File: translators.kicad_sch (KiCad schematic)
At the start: 56 parts, among them Q5 DMG1012T-7, U12 SN74AXC8T245RJWR, U2 SN74AXC8T245RJWR, U3 SN74AXC8T245RJWR, U4 SN74AXC8T245RJWR, U5 SN74AXC8T245RJWR, U6 SN74AXC8T245RJWR

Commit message: [#52835] schematics: update LPDDR5 connections, finish translators subsheet
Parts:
- removed C23, C24, C25, C27, C28, C29: C_1u_0402, antmicro-footprints:C_0402_1005Metric, symbol antmicroCapacitors0402:C_1u_0402
- removed Q5: DMG1012T-7, antmicro-footprints:SOT-523, symbol antmicroTransistorsFETsMOSFETsSingle:DMG1012T-7
- removed R1, R10, R2, R3, R4, R5, R50, R51, R52, R53, R54, R55, R6, R9: 4x0R_0402_array, antmicro-footprints:4x0R_0402_array_EXB28V, symbol antmicroResistorNetworksArrays:4x0R_0402_array
- removed R20, R59, R62, R67: R_0R_0402, antmicro-footprints:R_0402_1005Metric, symbol antmicroResistors0402:R_0R_0402
- removed R70, R71: R_1k_0402, antmicro-footprints:R_0402_1005Metric, symbol antmicroResistors0402:R_1k_0402
- removed U2, U4, U5: SN74AXC8T245RJWR, antmicro-footprints:UQFN-28-2x4mm_P0.4mm_Texas_RJW0024A, symbol antmicroLogicTranslatorsLevelShifters:SN74AXC8T245RJWR
- added C? (x6): C_1u_0402, antmicro-footprints:C_0402_1005Metric, symbol antmicroCapacitors0402:C_1u_0402
- added R? (x14): 4x0R_0402_array, antmicro-footprints:4x0R_0402_array_EXB28V, symbol antmicroResistorNetworksArrays:4x0R_0402_array
- added R? (x4): R_0R_0402, antmicro-footprints:R_0402_1005Metric, symbol antmicroResistors0402:R_0R_0402
- added U? (x3): SN74AXC8T245RJWR, antmicro-footprints:UQFN-28-2x4mm_P0.4mm_Texas_RJW0024A, symbol antmicroLogicTranslatorsLevelShifters:SN74AXC8T245RJWR
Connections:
- net DQA_{VTI}0: now also R?.5 (R4.2), U?.9 (A8)
- net DQA_{VTI}1: now also R?.6 (R3.2), U?.8 (A7)
- net DQA_{VTI}10: now also R?.6 (R3.2), U?.4 (A3)
- net DQA_{VTI}11: now also R?.5 (R4.2), U?.5 (A4)
- net DQA_{VTI}12: now also R?.8 (R1.2), U?.6 (A5)
- net DQA_{VTI}13: now also R?.7 (R2.2), U?.7 (A6)
- net DQA_{VTI}14: now also R?.6 (R3.2), U?.8 (A7)
- net DQA_{VTI}15: now also R?.5 (R4.2), U?.9 (A8)
- net DQA_{VTI}2: now also R?.7 (R2.2), U?.7 (A6)
- net DQA_{VTI}3: now also R?.8 (R1.2), U?.6 (A5)
- net DQA_{VTI}4: now also R?.5 (R4.2), U?.5 (A4)
- net DQA_{VTI}5: now also R?.6 (R3.2), U?.4 (A3)
- net DQA_{VTI}6: now also R?.7 (R2.2), U?.3 (A2)
- net DQA_{VTI}7: now also R?.8 (R1.2), U?.2 (A1)
- net DQA_{VTI}8: now also R?.8 (R1.2), U?.2 (A1)
- net DQA_{VTI}9: now also R?.7 (R2.2), U?.3 (A2)
- net DQA_{VT}0: now also R?.4 (R4.1), U?.13 (B8)
- net DQA_{VT}1: now also R?.3 (R3.1), U?.14 (B7)
- net DQA_{VT}10: now also R?.3 (R3.1), U?.18 (B3)
- net DQA_{VT}11: now also R?.4 (R4.1), U?.17 (B4)
- net DQA_{VT}12: now also R?.1 (R1.1), U?.16 (B5)
- net DQA_{VT}13: now also R?.2 (R2.1), U?.15 (B6)
- net DQA_{VT}14: now also R?.3 (R3.1), U?.14 (B7)
- net DQA_{VT}15: now also R?.4 (R4.1), U?.13 (B8)
- net DQA_{VT}2: now also R?.2 (R2.1), U?.15 (B6)
- net DQA_{VT}3: now also R?.1 (R1.1), U?.16 (B5)
- net DQA_{VT}4: now also R?.4 (R4.1), U?.17 (B4)
- net DQA_{VT}5: now also R?.3 (R3.1), U?.18 (B3)
- net DQA_{VT}6: now also R?.2 (R2.1), U?.19 (B2)
- net DQA_{VT}7: now also R?.1 (R1.1), U?.20 (B1)
- net DQA_{VT}8: now also R?.1 (R1.1), U?.20 (B1)
- net DQA_{VT}9: now also R?.2 (R2.1), U?.19 (B2)
- net DQH_DIR: now also U?.1 (DIR1)
- net DQL_DIR: now also U?.1 (DIR1)
- net FPGA_VDDQ: now also C?.2, C?.2, C?.2, R?.2, U?.24 (VCCA), U?.24 (VCCA), U?.24 (VCCA)
- net GND: now also R61.2, C?.1, C?.1, C?.1, C?.1, C?.1, C?.1, R?.1 (R1.1), R?.2, R?.6 (R3.2), R?.7 (R2.2), R?.7 (R2.2), R?.8 (R1.2), R?.8 (R1.2), R?.8 (R1.2), U?.11 (GND), U?.11 (GND), U?.11 (GND), U?.12 (GND), U?.12 (GND), U?.12 (GND); no longer R61.1
- net VDD_TL: now also C?.2, C?.2, C?.2, U?.22 (VCCB), U?.22 (VCCB), U?.22 (VCCB), U?.23 (VCCB), U?.23 (VCCB), U?.23 (VCCB)
- net ~{TRANS_OE_2}: now also R?.2, U?.21 (OE_N), U?.21 (OE_N), U?.21 (OE_N)
- net ~{TRANS_OE}: now also R?.1
- net at R23.2: now also U?.10 (DIR2)
- net at U12.1 (DIR1): now also R?.1
- net at U12.10 (DIR2): now also R?.1
- net at U6.1 (DIR1): now also R61.1; no longer R61.2
- net at U6.14 (B7): now also R?.3 (R3.1)
- net at U6.15 (B6): now also R?.2 (R2.1)
- net at U6.16 (B5): now also R?.1 (R1.1)
- net at U6.19 (B2): now also R?.2 (R2.1)
- net at U6.20 (B1): now also R?.1 (R1.1)
- net at R22.2: now also U?.10 (DIR2)
- net at R21.2: now also U?.10 (DIR2)
- net CK_A_{VTI}_N renamed CK_{VTI}_N
- net CK_A_{VTI}_P renamed CK_{VTI}_P
- net CK_A_{VT}_N renamed CK_{VT}_N
- net CK_A_{VT}_P renamed CK_{VT}_P
- net CS_{VTI}_A0 renamed CS_{VTI}0
- net CS_{VTI}_A1 renamed CS_{VTI}1
- net CS_{VT}_A0 renamed CS_{VT}0
- net CS_{VT}_A1 renamed CS_{VT}1
- net DMI_A1_DIR renamed DMI1_DIR
- net DMI_{VTI}_A0 renamed DMI_{VTI}0
- net DMI_{VTI}_A1 renamed DMI_{VTI}1
- net DMI_{VT}_A0 renamed DMI_{VT}0
- net DMI_{VT}_A1 renamed DMI_{VT}1
- net DMI_{VT}1: now also R?.4 (R4.1)
- net LPDDR5.CK_A_N renamed LPDDR5.CK_N
- net LPDDR5.CK_A_P renamed LPDDR5.CK_P
- net LPDDR5.CS_A0 renamed LPDDR5.CS0
- net LPDDR5.CS_A1 renamed LPDDR5.CS1
- net LPDDR5.DMI_A0 renamed LPDDR5.DMI0
- net LPDDR5.RDQS_A_0_N renamed LPDDR5.RDQS0_N
- net LPDDR5.RDQS_A_0_P renamed LPDDR5.RDQS0_P
- net LPDDR5.WCK_A_0_N renamed LPDDR5.WCK0_N
- net LPDDR5.WCK_A_0_P renamed LPDDR5.WCK0_P
- net LPDDR5.WCK_A_1_N renamed LPDDR5.WCK1_N
- net LPDDR5.WCK_A_1_P renamed LPDDR5.WCK1_P
- net LPDDR5_HV.CK_A_N renamed LPDDR5_HV.CK_N
- net LPDDR5_HV.CK_A_P renamed LPDDR5_HV.CK_P
- net LPDDR5_HV.CS_A0 renamed LPDDR5_HV.CS0
- net LPDDR5_HV.CS_A1 renamed LPDDR5_HV.CS1
- net LPDDR5_HV.DMI_A0 renamed LPDDR5_HV.DMI0
- net LPDDR5_HV.DMI_A1 renamed LPDDR5_HV.DMI1
- net LPDDR5_HV.RDQS_A_0_N renamed LPDDR5_HV.RDQS0_N
- net LPDDR5_HV.RDQS_A_0_P renamed LPDDR5_HV.RDQS0_P
- net LPDDR5_HV.RDQS_A_1_N renamed LPDDR5_HV.RDQS1_N
- net LPDDR5_HV.RDQS_A_1_P renamed LPDDR5_HV.RDQS1_P
- net LPDDR5_HV.WCK_A_0_N renamed LPDDR5_HV.WCK0_N
- net LPDDR5_HV.WCK_A_0_P renamed LPDDR5_HV.WCK0_P
- net LPDDR5_HV.WCK_A_1_N renamed LPDDR5_HV.WCK1_N
- net LPDDR5_HV.WCK_A_1_P renamed LPDDR5_HV.WCK1_P
- net RDQS_{VTI}_A0_N renamed RDQS_{VTI}0_N
- net RDQS_{VTI}_A0_P renamed RDQS_{VTI}0_P
- net RDQS_{VTI}_A1_N renamed RDQS_{VTI}1_N
- net RDQS_{VTI}_A1_P renamed RDQS_{VTI}1_P
- net RDQS_{VT}_A0_N renamed RDQS_{VT}0_N
- net RDQS_{VT}_A0_P renamed RDQS_{VT}0_P
- net RDQS_{VT}_A1_N renamed RDQS_{VT}1_N
- net RDQS_{VT}1_N: now also R?.4 (R4.1)
- net RDQS_{VT}_A1_P renamed RDQS_{VT}1_P
- net RDQS_{VT}1_P: now also R?.3 (R3.1)
- net WCK_A0_{VTI}_N renamed WCK0_{VTI}_N
- net WCK_A0_{VTI}_P renamed WCK0_{VTI}_P
- net WCK_A0_{VT}_N renamed WCK0_{VT}_N
- net WCK_A0_{VT}_P renamed WCK0_{VT}_P
- net WCK_A1_{VTI}_N renamed WCK1_{VTI}_N
- net WCK_A1_{VTI}_P renamed WCK1_{VTI}_P
- net WCK_A1_{VT}_N renamed WCK1_{VT}_N
- net WCK_A1_{VT}_P renamed WCK1_{VT}_P
- new net: R?.1 (R1.1), U?.20 (B1)
- new net: R?.1, U?.1 (DIR1)
- new net: R?.8 (R1.2), U?.2 (A1)
- new net CA_{VTI}0: R?.5 (R4.2), U?.9 (A8)
- new net CA_{VTI}1: R?.6 (R3.2), U?.8 (A7)
- new net CA_{VTI}2: R?.7 (R2.2), U?.7 (A6)
- new net CA_{VTI}3: R?.5 (R4.2), U?.5 (A4)
- new net CA_{VTI}4: R?.8 (R1.2), U?.6 (A5)
- new net CA_{VTI}5: R?.7 (R2.2), U?.3 (A2)
- new net CA_{VTI}6: R?.6 (R3.2), U?.4 (A3)
- new net CA_{VT}0: R?.4 (R4.1), U?.13 (B8)
- new net CA_{VT}1: R?.3 (R3.1), U?.14 (B7)
- new net CA_{VT}2: R?.2 (R2.1), U?.15 (B6)
- new net CA_{VT}3: R?.4 (R4.1), U?.17 (B4)
- new net CA_{VT}4: R?.1 (R1.1), U?.16 (B5)
- new net CA_{VT}5: R?.2 (R2.1), U?.19 (B2)
- new net CA_{VT}6: R?.3 (R3.1), U?.18 (B3)
- new net DMI0_DIR: R?.2
- new net LPDDR5.CA0: R?.5 (R4.2)
- new net LPDDR5.CA1: R?.6 (R3.2)
- new net LPDDR5.CA2: R?.7 (R2.2)
- new net LPDDR5.CA3: R?.5 (R4.2)
- new net LPDDR5.CA4: R?.8 (R1.2)
- new net LPDDR5.CA5: R?.7 (R2.2)
- new net LPDDR5.CA6: R?.6 (R3.2)
- new net LPDDR5.DMI1: R?.5 (R4.2)
- new net LPDDR5.DQ0: R?.5 (R4.2)
- new net LPDDR5.DQ1: R?.6 (R3.2)
- new net LPDDR5.DQ10: R?.6 (R3.2)
- new net LPDDR5.DQ11: R?.5 (R4.2)
- new net LPDDR5.DQ12: R?.8 (R1.2)
- new net LPDDR5.DQ13: R?.7 (R2.2)
- new net LPDDR5.DQ14: R?.6 (R3.2)
- new net LPDDR5.DQ15: R?.5 (R4.2)
- new net LPDDR5.DQ2: R?.7 (R2.2)
- new net LPDDR5.DQ3: R?.8 (R1.2)
- new net LPDDR5.DQ4: R?.5 (R4.2)
- new net LPDDR5.DQ5: R?.6 (R3.2)
- new net LPDDR5.DQ6: R?.7 (R2.2)
- new net LPDDR5.DQ7: R?.8 (R1.2)
- new net LPDDR5.DQ8: R?.8 (R1.2)
- new net LPDDR5.DQ9: R?.7 (R2.2)
- new net LPDDR5.RDQS1_N: R?.5 (R4.2)
- new net LPDDR5.RDQS1_P: R?.6 (R3.2)
- new net LPDDR5_HV.CA0: R?.4 (R4.1)
- new net LPDDR5_HV.CA1: R?.3 (R3.1)
- new net LPDDR5_HV.CA2: R?.2 (R2.1)
- new net LPDDR5_HV.CA3: R?.4 (R4.1)
- new net LPDDR5_HV.CA4: R?.1 (R1.1)
- new net LPDDR5_HV.CA5: R?.2 (R2.1)
- new net LPDDR5_HV.CA6: R?.3 (R3.1)
- new net LPDDR5_HV.DQ0: R?.4 (R4.1)
- new net LPDDR5_HV.DQ1: R?.3 (R3.1)
- new net LPDDR5_HV.DQ10: R?.3 (R3.1)
- new net LPDDR5_HV.DQ11: R?.4 (R4.1)
- new net LPDDR5_HV.DQ12: R?.1 (R1.1)
- new net LPDDR5_HV.DQ13: R?.2 (R2.1)
- new net LPDDR5_HV.DQ14: R?.3 (R3.1)
- new net LPDDR5_HV.DQ15: R?.4 (R4.1)
- new net LPDDR5_HV.DQ2: R?.2 (R2.1)
- new net LPDDR5_HV.DQ3: R?.1 (R1.1)
- new net LPDDR5_HV.DQ4: R?.4 (R4.1)
- new net LPDDR5_HV.DQ5: R?.3 (R3.1)
- new net LPDDR5_HV.DQ6: R?.2 (R2.1)
- new net LPDDR5_HV.DQ7: R?.1 (R1.1)
- new net LPDDR5_HV.DQ8: R?.1 (R1.1)
- new net LPDDR5_HV.DQ9: R?.2 (R2.1)
- no-connect marks 2 -> 1
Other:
- note added: "DMI0"
- note added: "DMI0_DIR"
- note added: "DMI1"
- note added: "RDQS_0"
- note added: "RDQS_1"
- note added: "WCK, CS, CK, WCK"
- note removed: "DMI_A0"
- note removed: "DMI_A0_DIR"
- note removed: "DMI_A1"
- note removed: "RDQS_A_0"
- note removed: "RDQS_A_1"
- note removed: "WCK, CS, CK_A, WCK_A"
- moved on the sheet: C26, C30, C31, C32, C33, C34, R21, R22, R23, R48, R49, R56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

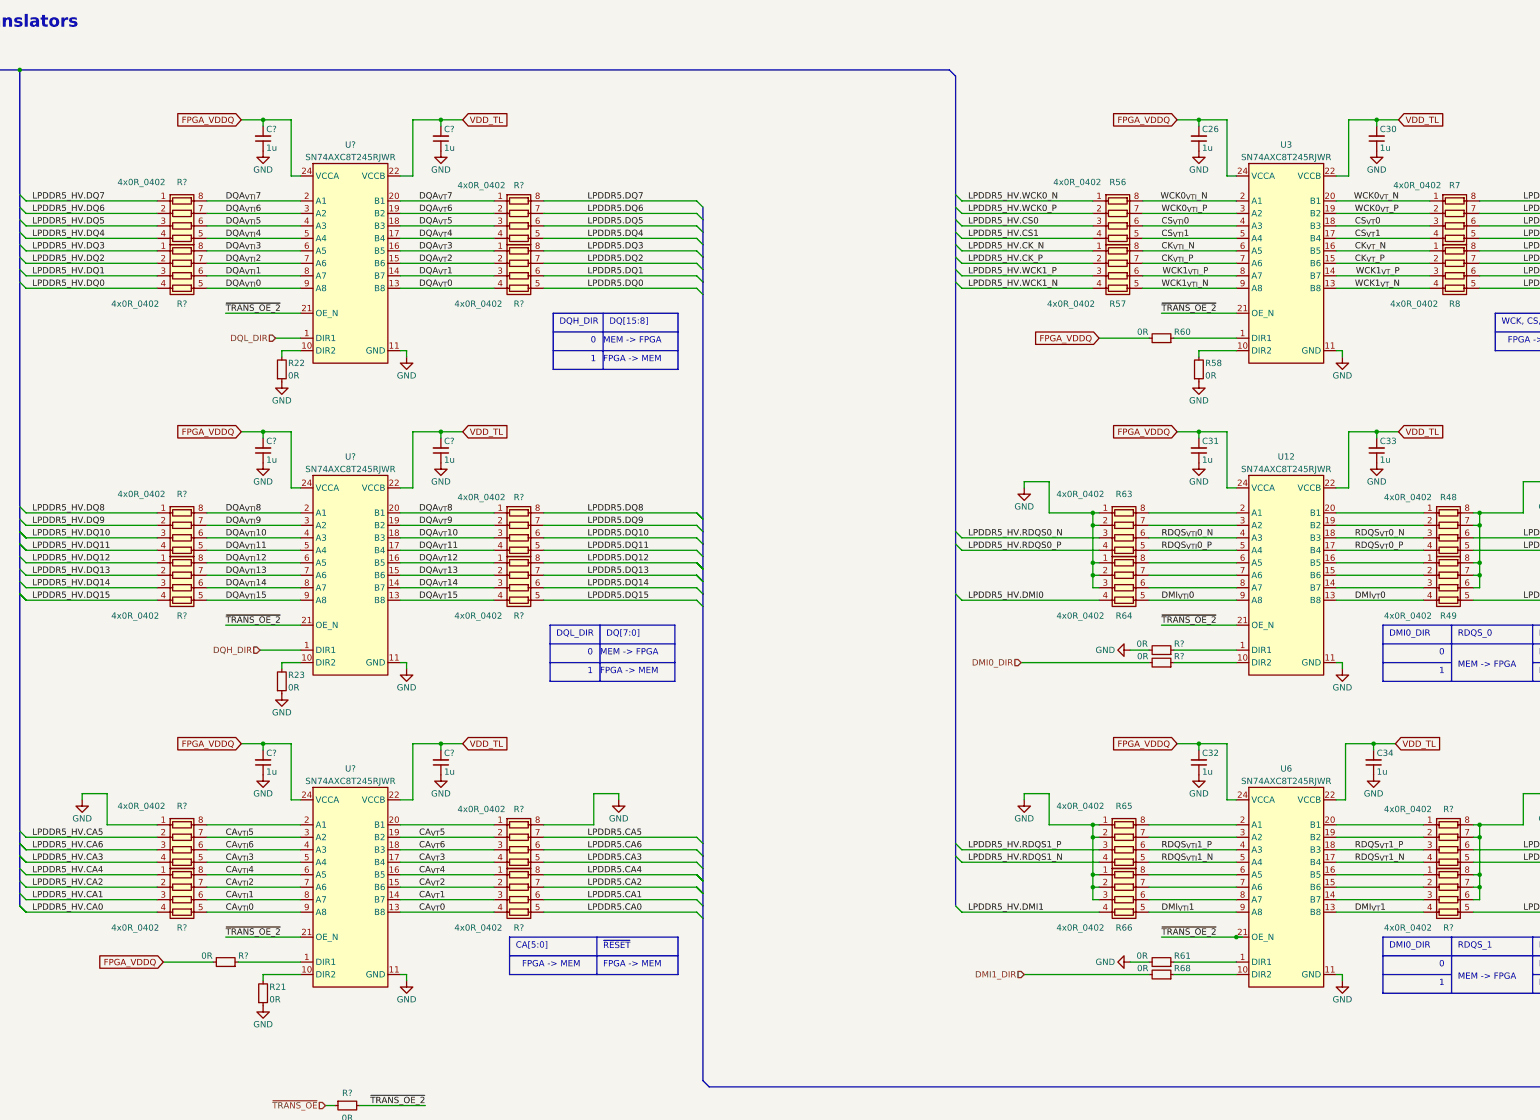
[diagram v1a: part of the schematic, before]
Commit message: [#52536] schematics: update I2C connection
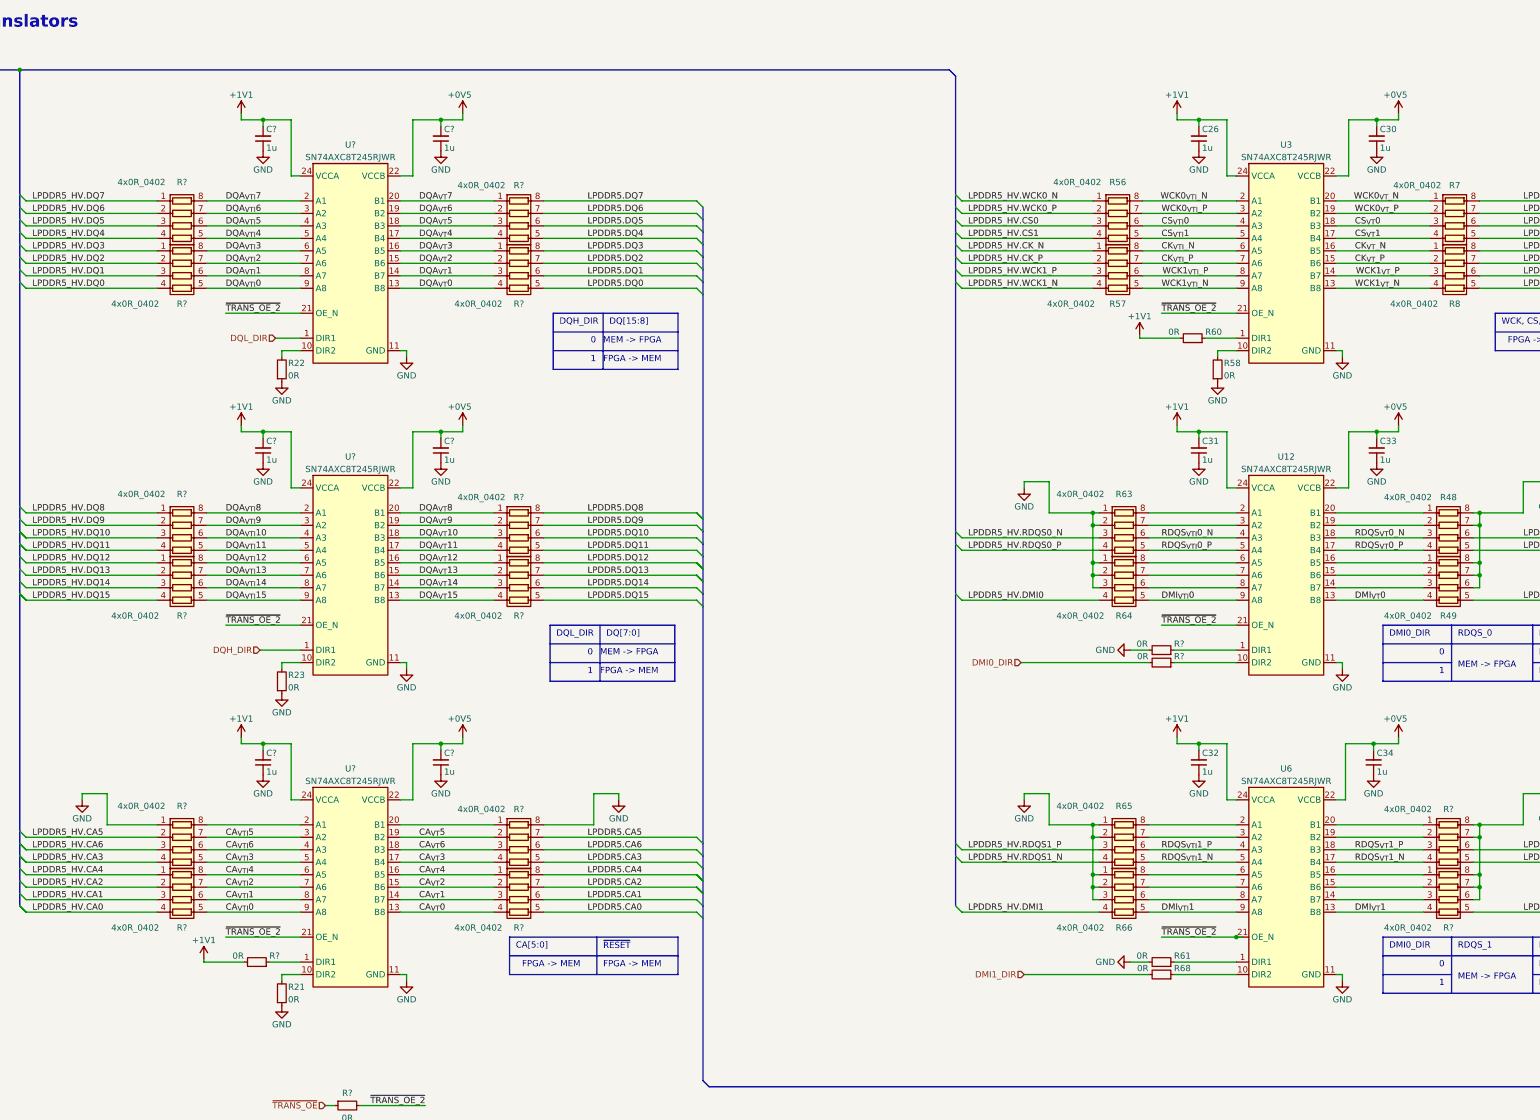
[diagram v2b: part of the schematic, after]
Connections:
- net FPGA_VDDQ renamed +1V1
- net VDD_TL renamed +0V5
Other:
- moved on the sheet: R21, R58, R60, R?
